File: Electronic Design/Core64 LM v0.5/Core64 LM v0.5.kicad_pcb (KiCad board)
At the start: 2 copper layers, 85 x 85 mm, 76 parts, among them J1 Digi-Key 77311-420-36LF-ND, J2 Digi-Key 77311-420-36LF-ND, J3 Conn_01x03_Male

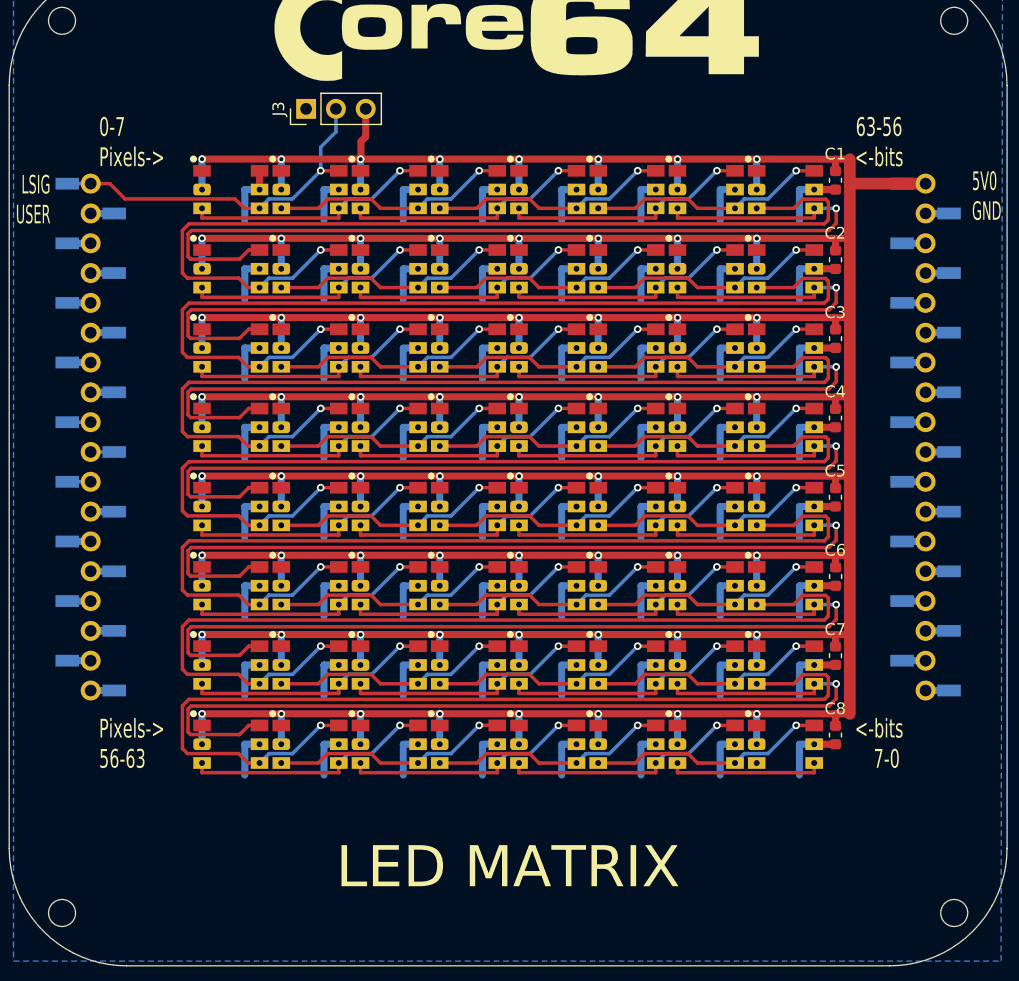
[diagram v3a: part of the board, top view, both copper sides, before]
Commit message: Refine LED Matrix board silk screen details
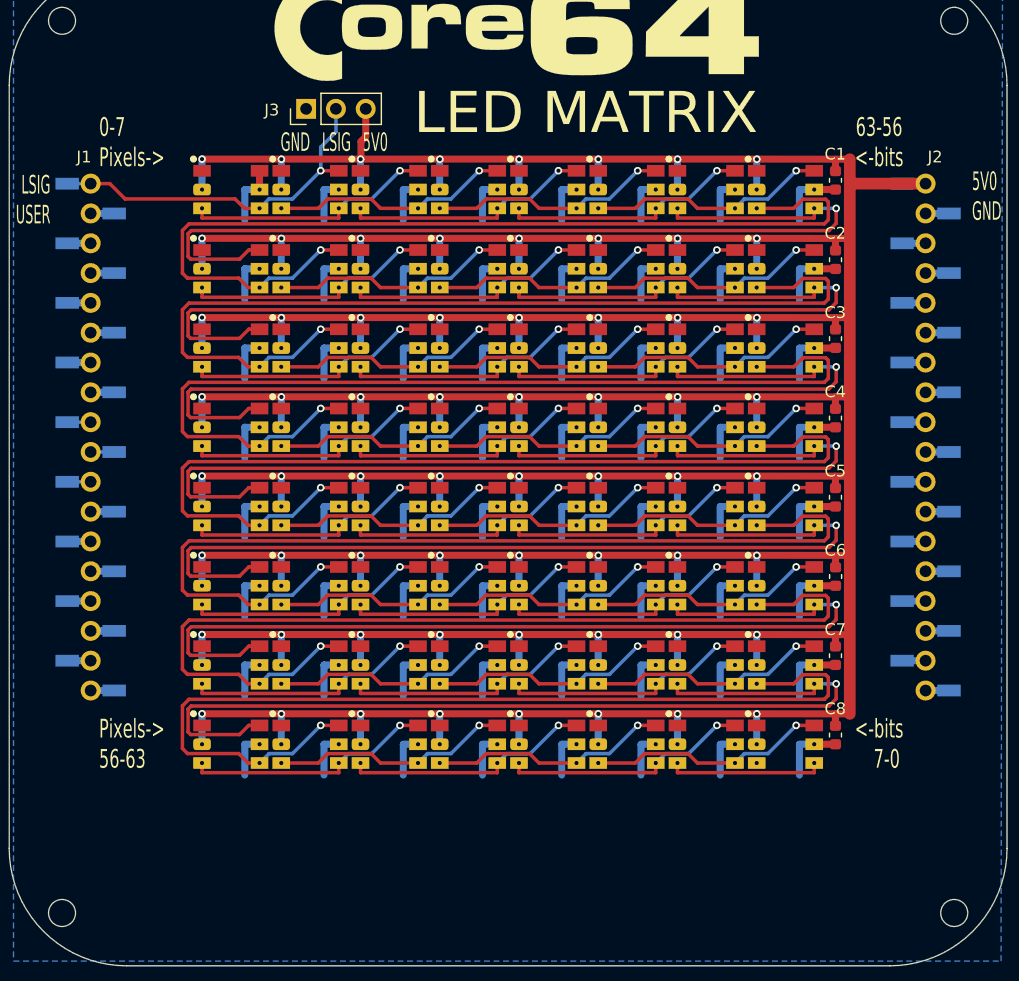
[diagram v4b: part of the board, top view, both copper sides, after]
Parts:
- added ?: , , F.Cu at (-99.1, -32.6)
- added ?: , , F.Cu at (74.6, 0.85)
- added ?: , , F.Cu at (-36.4, -29.1)
- D1, D10, D11, D12, D13, D14, D15, D16, D17, D18, D19, D2, D20, D21, D22, D23, D24, D25, D26, D27, D28, D29, D3, D30, D31, D32, D33, D34, D35, D36, D37, D38, D39, D4, D40, D41, D42, D43, D44, D45, D46, D47, D48, D49, D5, D50, D51, D52, D53, D54, D55, D56, D57, D58, D59, D6, D60, D61, D62, D63, D64, D7, D8, D9: value WS2813C -> WS2813
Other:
- board text added: "5V0"
- board text added: "CORE64 LED MATRIX (LM) V0.5 2021-02-12 Project information at www.Core64.io Designed by Andy Geppert at www.MachineIdeas.com WS2813 LEDs"
- board text added: "GND"
- board text added: "LSIG"
- board text removed: "LED MATRIX V0.5 2021-02-10 ANDY GEPPERT WWW.MACHINEIDEAS.COM"
